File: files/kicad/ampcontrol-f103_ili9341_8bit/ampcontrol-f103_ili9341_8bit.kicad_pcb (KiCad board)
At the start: 2 copper layers, 94.4 x 64.8 mm, 59 parts, among them J1 Audio, J12 TFT, J13 I2C_Audio, J14 I2C_Tuner, J15 I2C_Ext, J2 MUTE_STBY, J3 UART, J4 USB, J5 UART2, J6 UART3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

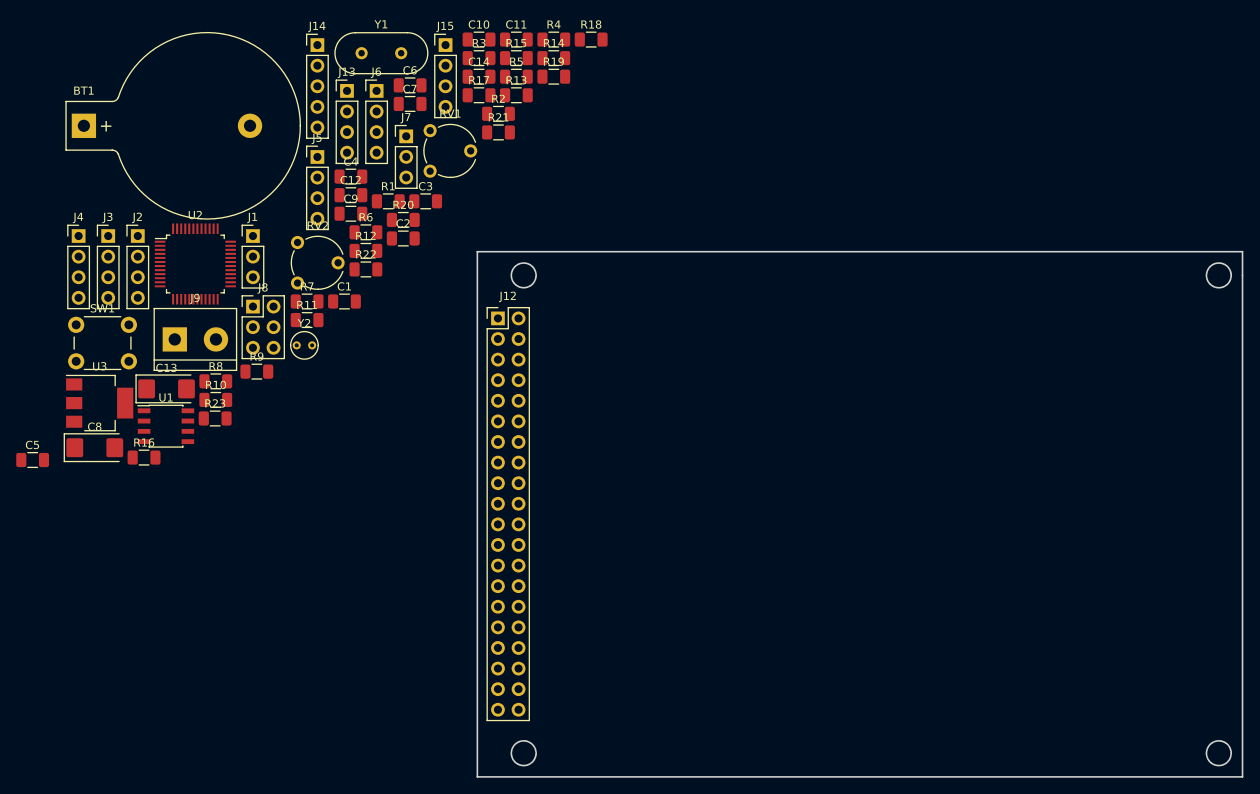
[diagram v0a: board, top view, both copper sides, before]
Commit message: Arrange components on PCB
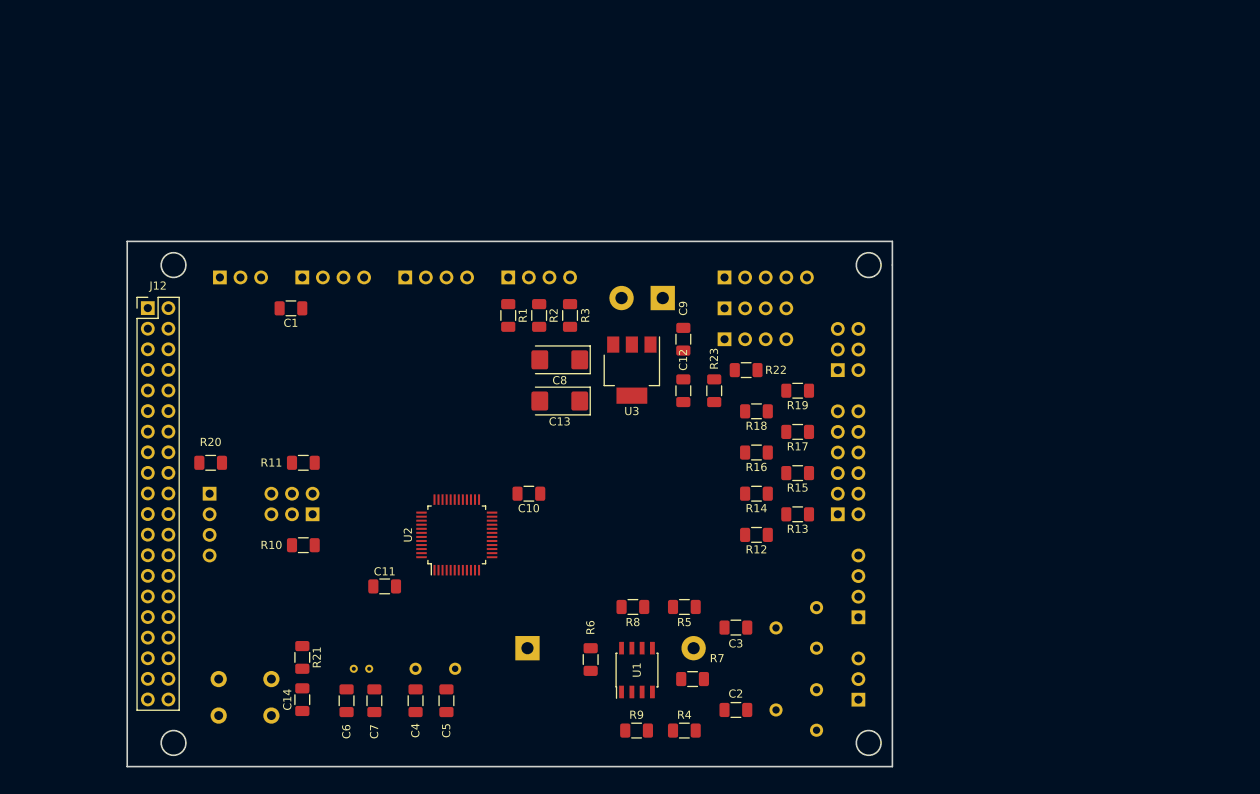
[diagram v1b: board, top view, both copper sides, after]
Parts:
- added J10: Buttons, Connector_PinHeader_2.54mm:PinHeader_2x06_P2.54mm_Vertical, B.Cu at (179.1, 105.4)
- added J11: Encoder, Connector_PinHeader_2.54mm:PinHeader_2x03_P2.54mm_Vertical, B.Cu at (179.1, 87.6)
- BT1, J1, J13, J14, J15, J2, J3, J4, J5, J6, J7, J8, J9, RV1, RV2, SW1, Y1, Y2: moved to B.Cu
- C13, C8: value CP -> 22.0
- R22, R23: value 4k7 -> 4.7k
- moved J1 94.0 mm to (181.6, 128.3)
- moved J5 87.6 mm to (181.6, 118.1)
- moved R4 86.7 mm to (160.2, 132.1), turned to 180 degrees
- moved BT1 84.5 mm to (140.8, 121.9)
- moved RV1 83.8 mm to (176.4, 132.0), turned to 180 degrees
- moved C14 79.9 mm to (113.0, 128.3), turned to 90 degrees
- moved RV2 78.3 mm to (176.4, 121.9), turned to 180 degrees
- moved Y1 76.8 mm to (131.9, 124.5), turned to 180 degrees
- moved C6 76.3 mm to (118.5, 128.4), turned to 270 degrees
- moved R16 75.5 mm to (169.0, 97.8), turned to 180 degrees
- moved C7 73.7 mm to (121.9, 128.4), turned to 90 degrees
- moved C2 71.2 mm to (166.5, 129.5)
- moved C11 69.4 mm to (123.2, 114.3)
- moved R21 69.1 mm to (113.0, 123.1), turned to 270 degrees
- moved R5 68.6 mm to (160.2, 116.8), turned to 180 degrees
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
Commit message: Testing autorouted board
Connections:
- net Net-(BT1-Pad1) renamed /VBAT
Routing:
- net GNDD: track 0.00 -> 424.8 mm, vias 0 -> 1
- net +3V3: track 0.00 -> 362.2 mm, vias 0 -> 2
- net /DB7: track 0.00 -> 154.5 mm, vias 0 -> 1
- net /DB0: track 0.00 -> 141.2 mm, vias 0 -> 1
- net /DB6: track 0.00 -> 138.1 mm, vias 0 -> 1
- net /DB2: track 0.00 -> 96.1 mm, vias 0 -> 2
- net /DB1: track 0.00 -> 94.5 mm, vias 0 -> 2
- net /DB5: track 0.00 -> 87.2 mm
- net /DB3: track 0.00 -> 86.7 mm, vias 0 -> 2
- net /DB4: track 0.00 -> 83.2 mm, vias 0 -> 2
- net /SCL: track 0.00 -> 68.5 mm, vias 0 -> 1
- net /SDA: track 0.00 -> 65.4 mm, vias 0 -> 1
- net +5V: track 0.00 -> 63.3 mm
- net /HW_RST: track 0.00 -> 60.1 mm, vias 0 -> 1
- net /NRST: track 0.00 -> 55.2 mm, vias 0 -> 1
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- added copper zone on B.Cu, net GNDD
- added copper zone on F.Cu, net GNDD
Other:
- net class Power added: clearance 0.2, trace_width 0.4, via_dia 0.8, via_drill 0.4

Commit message: Change boot configuration no schematic
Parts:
- added Q1: BSS138, Package_TO_SOT_SMD:SOT-23, F.Cu at (109.2, 105.4)
- J8: footprint Connector_PinHeader_2.54mm:PinHeader_2x03_P2.54mm_Vertical -> Connector_PinHeader_2.54mm:PinHeader_1x02_P2.54mm_Vertical; moved to F.Cu
- moved J8 5.68 mm to (111.8, 110.5), turned to 270 degrees
- moved R10 5.21 mm to (114.3, 104.1)
- moved R11 1.71 mm to (114.3, 100.3), turned to 180 degrees
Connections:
- J8 pad 1: +3V3 -> /BOOT0
- J8 pad 2: +3V3 -> GNDD
- R10 pad 1: /BOOT0 -> +3V3
- R10 pad 2: Net-(J8-Pad3) -> /BOOT0
- R11 pad 1: Net-(J8-Pad4) -> +3V3
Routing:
- net GNDD: track 424.8 -> 0.00 mm, vias 1 -> 0
- net +3V3: track 362.2 -> 0.00 mm, vias 2 -> 0
- net /DB7: track 154.5 -> 0.00 mm, vias 1 -> 0
- net /DB0: track 141.2 -> 0.00 mm, vias 1 -> 0
- net /DB6: track 138.1 -> 0.00 mm, vias 1 -> 0
- net /DB2: track 96.1 -> 0.00 mm, vias 2 -> 0
- net /DB1: track 94.5 -> 0.00 mm, vias 2 -> 0
- net /DB5: track 87.2 -> 0.00 mm
- net /DB3: track 86.7 -> 0.00 mm, vias 2 -> 0
- net /DB4: track 83.2 -> 0.00 mm, vias 2 -> 0
- net /SCL: track 68.5 -> 0.00 mm, vias 1 -> 0
- net /SDA: track 65.4 -> 0.00 mm, vias 1 -> 0
- net +5V: track 63.3 -> 0.00 mm
- net /HW_RST: track 60.1 -> 0.00 mm, vias 1 -> 0
- net /NRST: track 55.2 -> 0.00 mm, vias 1 -> 0
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- removed copper zone on B.Cu, net GNDD
- removed copper zone on F.Cu, net GNDD
